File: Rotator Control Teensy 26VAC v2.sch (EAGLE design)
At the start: 61 parts, among them K4 G5LE, K5 G5LE, K6 G5LE, Q1 BSS123, Q2 BSS123, Q3 BSS123

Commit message: add 5V LED, polishing
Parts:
- removed 12VDC, 36VDC, BRAKE, DIR, MOTOR: (no value), led:LED3MM
- removed K4, K5, K6: G5LE, relay:G5LE
- removed R103, R104: 1k, rcl:R-US_R0805
- added K1, K2, K3: G5LE, relay:G5LE
- added LED1: Motor, led:LED3MM
- added LED2: Dir, led:LED3MM
- added LED3: Brake, led:LED3MM
- added LED4: 36V, led:LED3MM
- added LED5: 12V, led:LED3MM
- added LED6: 5V, led:LED3MM
- added R18: 500, rcl:R-US_R0805
- added R19, R20: 1k, rcl:R-US_R0805
- C19: value (none) -> 100u
- C2: device rcl:CPOL-USE7.5-18 -> rcl:CPOL-USE10-22.5
- D4, D5, D6: value (none) -> 1N4148
- X1: value (none) -> Rotor
- X2: value (none) -> 26VAC
- renumbered R102 to R21, U$3 to C19
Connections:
- net N$19 renamed CAP2
- net N$2 renamed N/C
- removed net +5V: U$1.VIN
- new net +12V1: R18.2, U$1.VIN
- new net N$2: LED6.A, R18.1
- net +12V: now also K11.1, K21.1, K31.1; no longer K41.1, K51.1, K61.1
- net +3V3: no longer U$1.3V3_LO
- net 26VAC: now also K12.P, K32.P; no longer K42.P, K62.P
- net BRAKE: now also K32.S; no longer K62.S
- net GND: now also LED4.C, LED5.C, LED6.C; no longer 12VDC.C, 36VDC.C
- net LEFT: now also C4.1, K22.O, R6.1, X1-6.1; no longer C3.1, K52.S, R5.1, X1-5.1
- net N$1: now also R20.2; no longer R104.2
- net N$10: now also K21.2, LED2.C; no longer DIR.C, K51.2
- net N$11: now also K31.2, LED3.C; no longer BRAKE.C, K61.2
- net N$15: now also LED4.A; no longer 36VDC.A
- net N$16: now also LED5.A; no longer 12VDC.A
- net N$3: now also R19.2; no longer R103.2
- net N$4: now also LED1.A; no longer MOTOR.A
- net N$5: now also LED2.A; no longer DIR.A
- net N$6: now also LED3.A; no longer BRAKE.A
- net N$8: now also K12.S, K22.P; no longer K42.S, K52.P
- net N$9: now also K11.2, LED1.C; no longer K41.2, MOTOR.C
- net RIGHT: now also C3.1, K22.S, R5.1, X1-5.1; no longer C4.1, K52.O, R6.1, X1-6.1
- net WIPER+: now also R19.1; no longer R103.1
- net WIPER-: now also R20.1; no longer R104.1
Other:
- note removed: "Cap 130 uFd"
- moved on the sheet: C13, C14, C15, C16, C17, C18, D2, D3, D4, D5, D6, Q1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

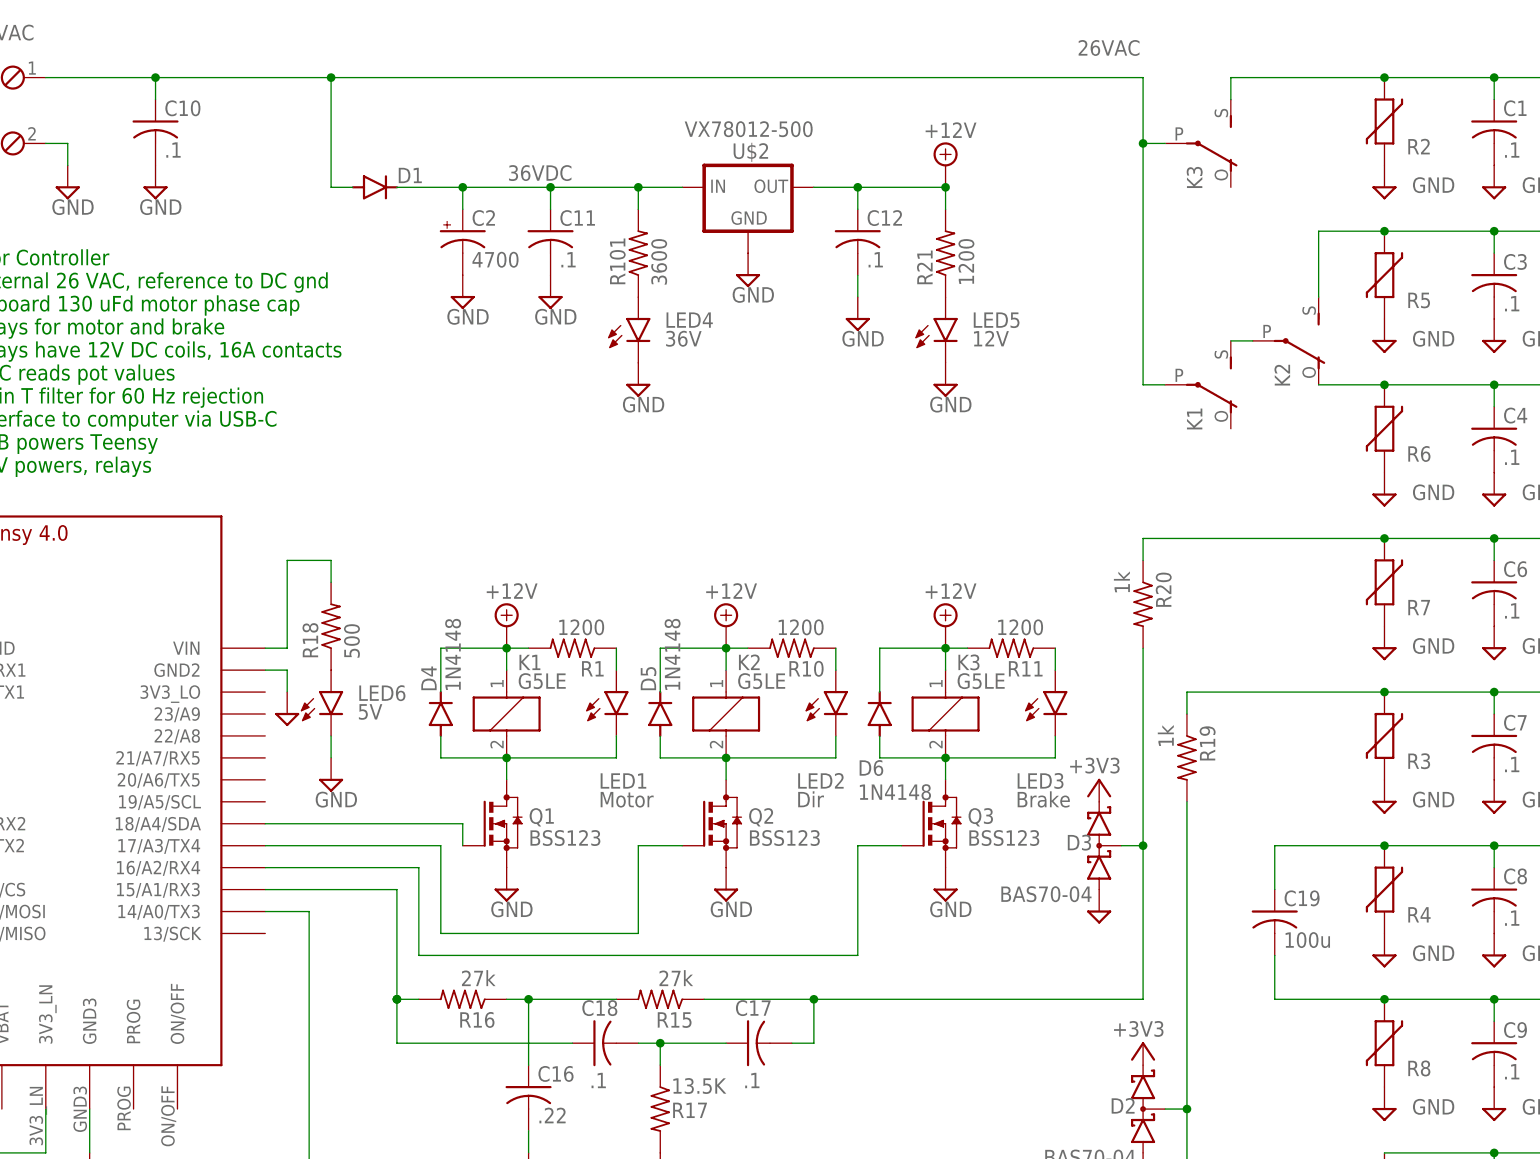
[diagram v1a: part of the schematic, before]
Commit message: Simplified by running relays from 5V from USB 26V AC is only for the rotator
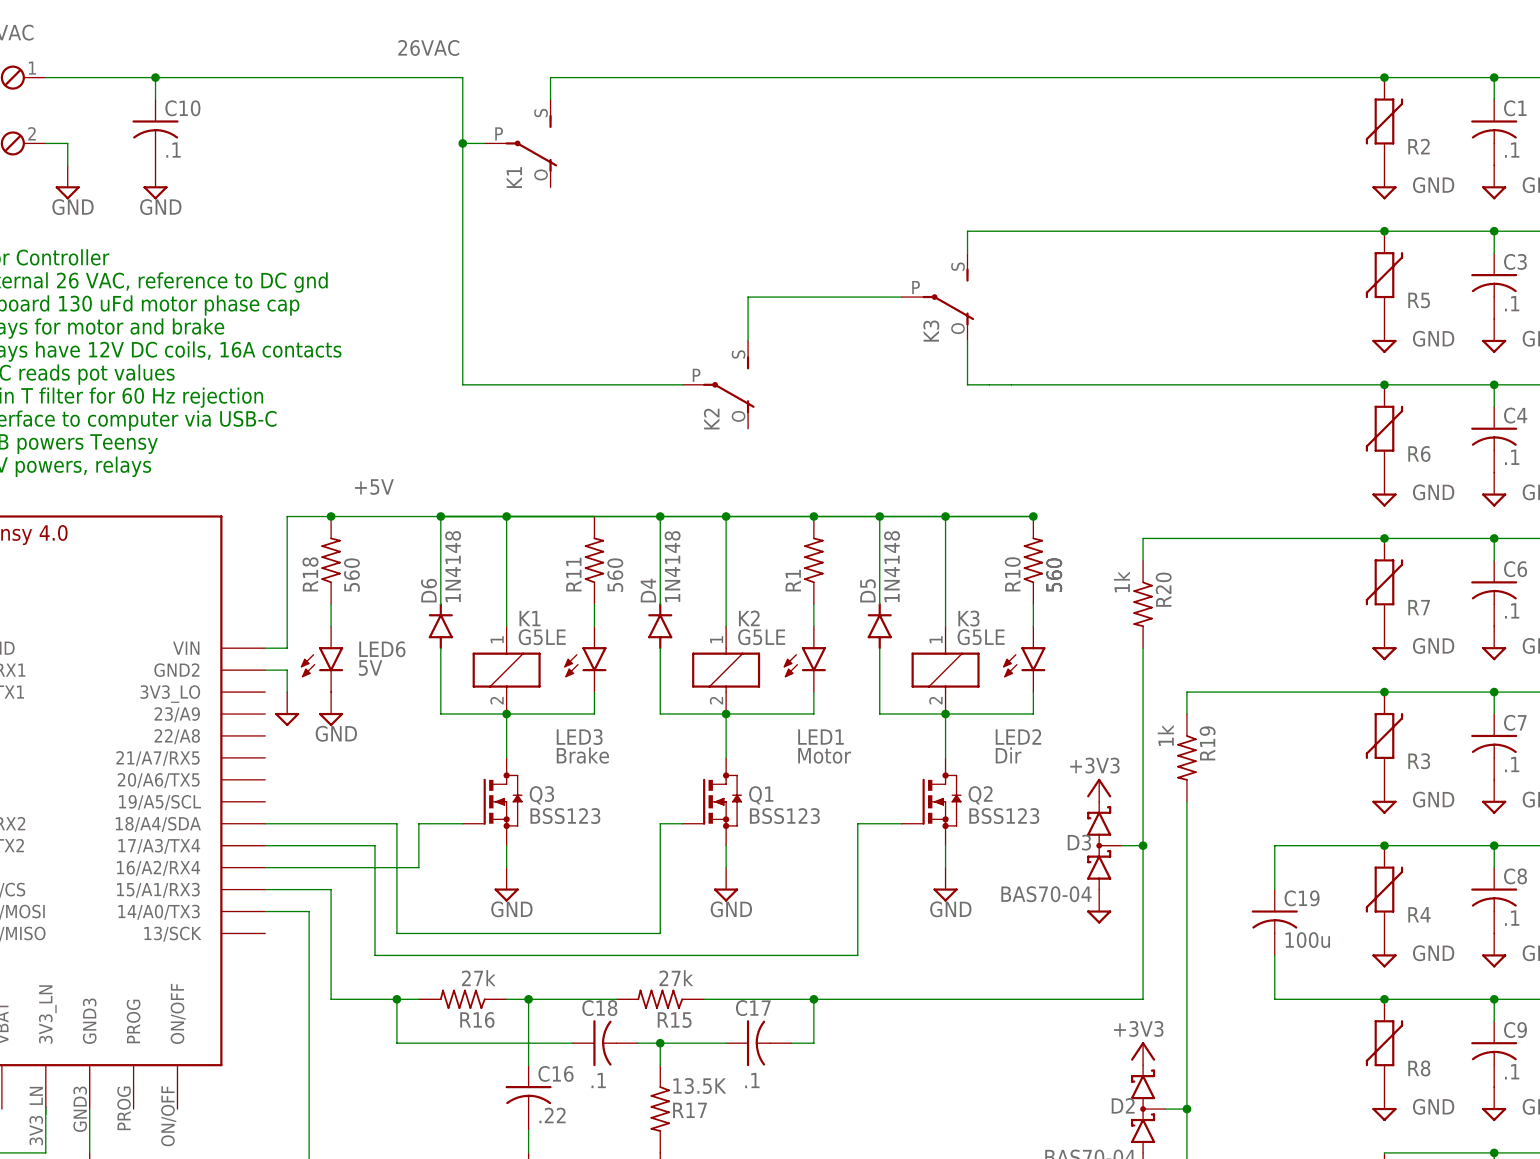
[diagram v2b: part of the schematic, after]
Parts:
- removed C11, C12: .1, rcl:C-USC1206
- removed C2: 4700, rcl:CPOL-USE10-22.5
- removed D1: 1N4148, diode:DIODE-DO214AC
- removed LED4: 36V, led:LED3MM
- removed LED5: 12V, led:LED3MM
- removed R101: 3600, rcl:R-US_R0805
- removed R21: 1200, rcl:R-US_R0805
- removed U$2: VX78012-500, my-library:VX78012-500
- R1, R10, R11: value 1200 -> 560
- R18: value 500 -> 560
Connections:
- removed net +12V: C12.1, D4.C, D5.C, D6.C, K11.1, K21.1, K31.1, R1.2, R10.2, R11.2, R21.2, U$2.OUT
- removed net +12V1: R18.2, U$1.VIN
- removed net 36VDC: C11.1, C2.+, D1.C, R101.2, U$2.IN
- removed net N$15: LED4.A, R101.1
- removed net N$16: LED5.A, R21.1
- new net +5V: D4.C, D5.C, D6.C, K11.1, K21.1, K31.1, R1.2, R10.2, R11.2, R18.2, U$1.VIN
- net 26VAC: now also K22.P; no longer D1.A, K32.P
- net BRAKE: now also K12.S; no longer K32.S
- net GND: no longer C11.2, C12.2, C2.-, LED4.C, LED5.C, U$2.GND
- net LEFT: now also K32.O; no longer K22.O
- net N$10: now also K31.2; no longer K21.2
- net N$11: now also K11.2; no longer K31.2
- net N$8: now also K22.S, K32.P; no longer K12.S, K22.P
- net N$9: now also K21.2; no longer K11.2
- net RIGHT: now also K32.S; no longer K22.S
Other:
- moved on the sheet: D4, D5, D6, K1, K2, K3, LED1, LED2, LED3, LED6, Q1, Q2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

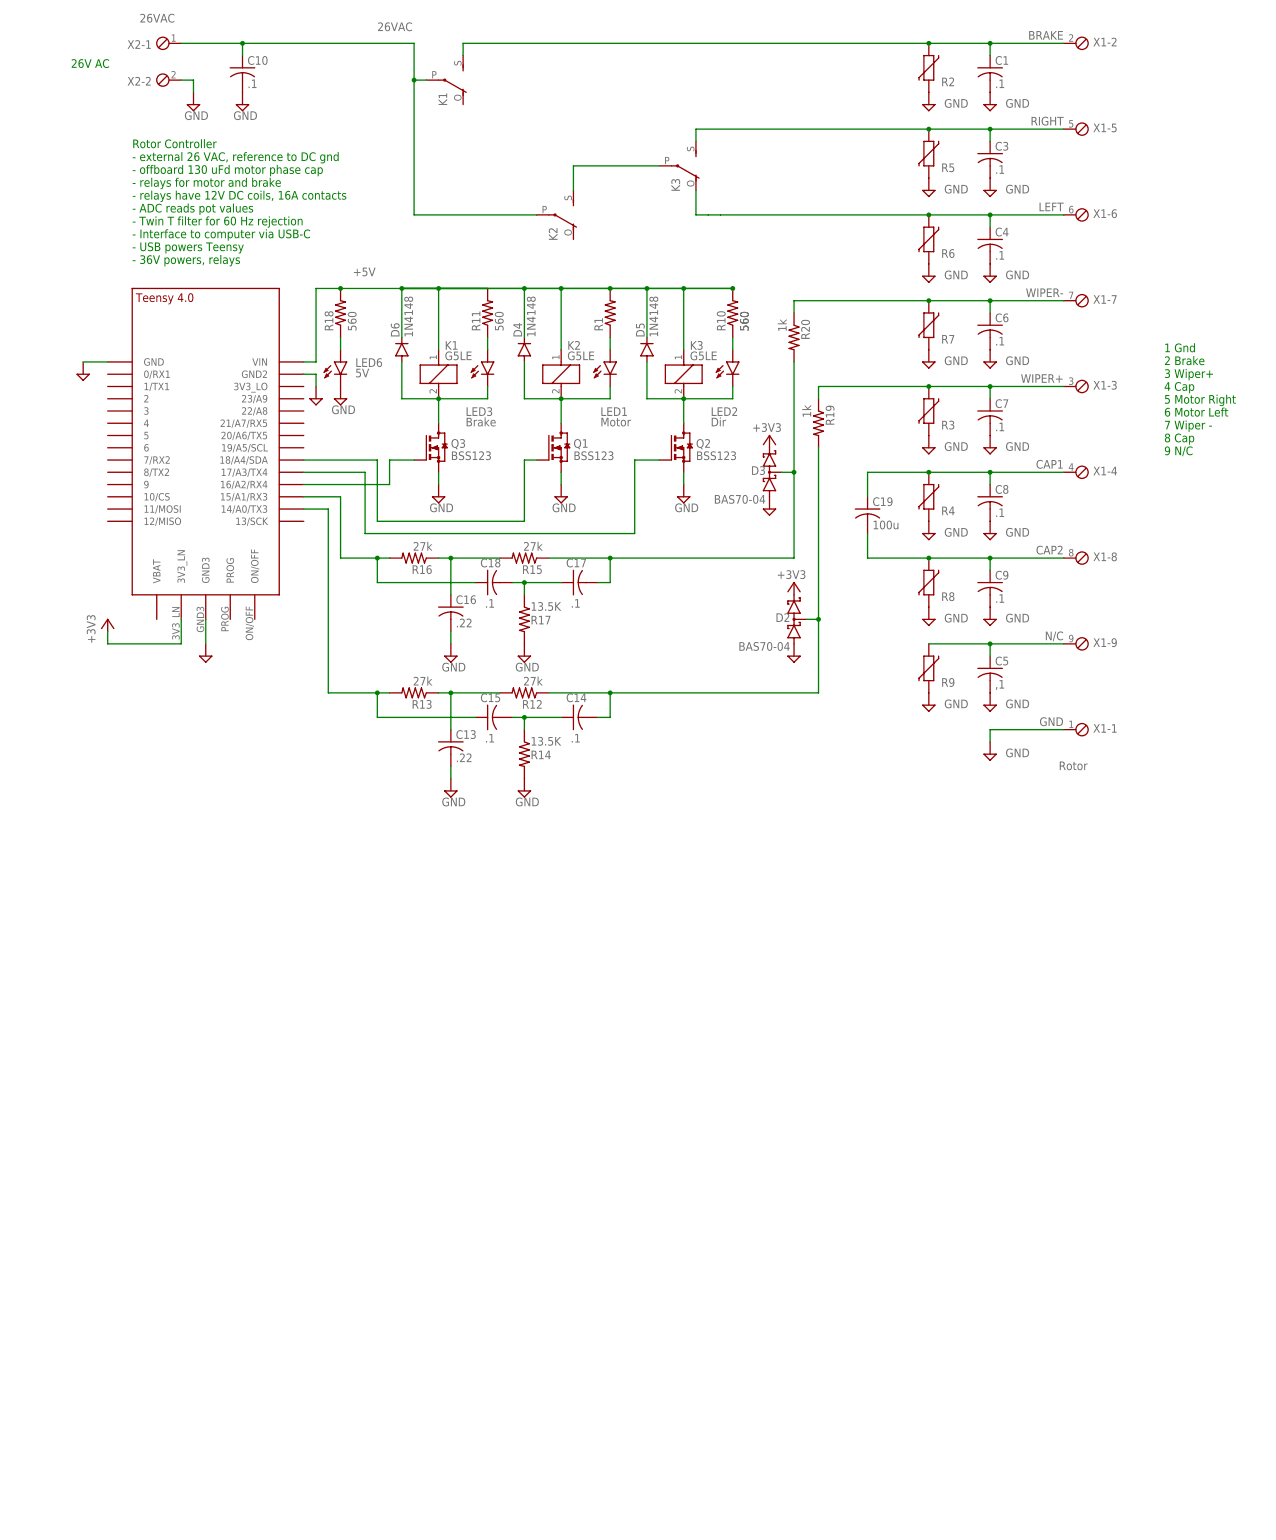
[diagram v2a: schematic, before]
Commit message: switched LED to -.28 inch 4 digit plus driver with keyswitch capability
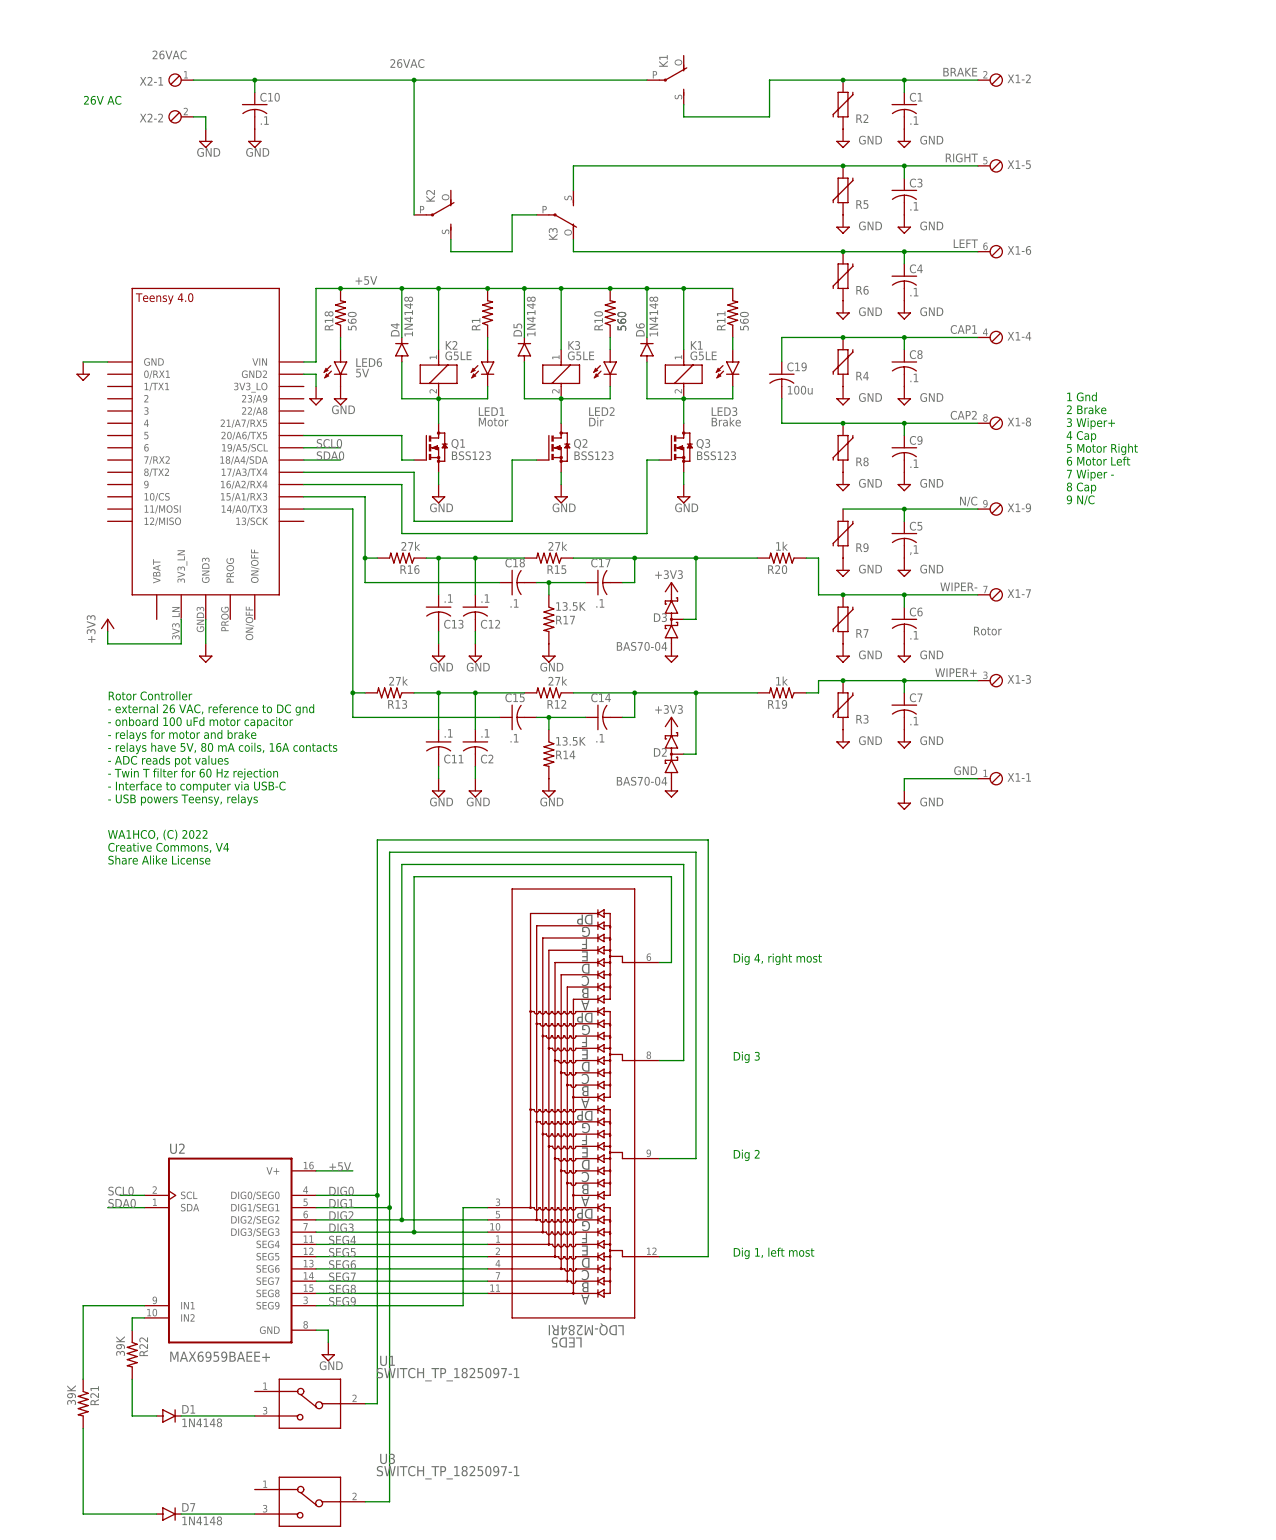
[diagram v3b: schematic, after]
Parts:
- removed C16: .22, rcl:C-USC1206
- added C11, C12, C2: .1, rcl:C-USC1206
- added D1, D7: 1N4148, diode:DIODE-DO214AC
- added LED5: LDQ-M284RI, my-library:LDQ-M284RI
- added R21, R22: 39K, rcl:R-US_R0805
- added U1, U3: SWITCH_TP_1825097-1, my-library:SWITCH_TP_1825097-1
- added U2: MAX6959BAEE+, MAX6959BAEE_:MAX6959BAEE+
- C13: value .22 -> .1
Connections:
- new net DIG0: LED5.12, U1.3, U2.DIG0/SEG0
- new net DIG1: LED5.9, U2.DIG1/SEG1, U3.3
- new net DIG2: LED5.5, LED5.8, U2.DIG2/SEG2
- new net DIG3: LED5.10, LED5.6, U2.DIG3/SEG3
- new net N$15: R21.1, U2.IN1
- new net N$16: R22.1, U2.IN2
- new net N$19: D7.A, R21.2
- new net N$20: D1.A, R22.2
- new net N$24: D1.C, U1.2
- new net N$25: D7.C, U3.2
- new net SCL0: U$1.19/A5/SCL, U2.SCL
- new net SDA0: U$1.18/A4/SDA, U2.SDA
- new net SEG4: LED5.1, U2.SEG4
- new net SEG5: LED5.2, U2.SEG5
- new net SEG6: LED5.4, U2.SEG6
- new net SEG7: LED5.7, U2.SEG7
- new net SEG8: LED5.11, U2.SEG8
- new net SEG9: LED5.3, U2.SEG9
- net +5V: now also U2.V+
- net GND: now also C11.2, C12.2, C2.2, U2.GND; no longer C16.2
- net N$13: now also U$1.20/A6/TX5; no longer U$1.18/A4/SDA
- net N$17: now also C11.1, C2.1; no longer C13.1
- net N$21: now also C12.1, C13.1; no longer C16.1
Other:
- note added: "Dig 1, left most"
- note added: "Dig 2"
- note added: "Dig 3"
- note added: "Dig 4, right most"
- note added: "Rotor Controller - external 26 VAC, reference to DC gnd - onboard 100 uFd motor capacitor - relays for motor and brake - relays have 5V, 80 mA coils, 16A contacts - ADC reads pot values - Twin T filter for 60 Hz rejection - Interface to computer via USB-C - USB powers Teensy, relays"
- note added: "WA1HCO, (C) 2022 Creative Commons, V4 Share Alike License"
- note removed: "Rotor Controller - external 26 VAC, reference to DC gnd - offboard 130 uFd motor phase cap - relays for motor and brake - relays have 12V DC coils, 16A contacts - ADC reads pot values - Twin T filter for 60 Hz rejection - Interface to computer via USB-C - USB powers Teensy - 36V powers, relays"
- moved on the sheet: C1, C10, C13, C14, C15, C17, C18, C19, C3, C4, C5, C6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

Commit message: Released this version to OshPark for fab
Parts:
- removed D7: 1N4148, diode:DIODE-DO214AC
- removed R5, R6, R8, R9: VARISTORCN1206, varistor:VARISTORCN1206
- removed U1, U3: SWITCH_TP_1825097-1, my-library:SWITCH_TP_1825097-1
- added C16: .1, rcl:C-USC1206
- added LED4: 26VAC, led:LED3MM
- added U$2, U$3: SWITCH_AEXIT_6X6X9.5, my-library:SWITCH_AEXIT_6X6X9.5
- D1, D4, D5, D6: device diode:DIODE-DO214AC -> adafruit:DIODESOD-123
- R4: value VARISTORCN1206 -> 3600; device varistor:VARISTORCN1206 -> rcl:R-US_R0805
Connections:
- net +5V: now also C16.1
- net 26VAC: now also D1.A, R2.1
- net BRAKE: no longer R2.1
- net CAP1: no longer R4.1
- net CAP2: no longer R8.1
- net DIG0: now also U$2.P$1, U$3.P$1; no longer U1.3
- net DIG1: no longer U3.3
- net GND: now also C16.2, LED4.C; no longer R4.2, R5.2, R6.2, R8.2, R9.2
- net LEFT: no longer R6.1
- net N$19: now also U$3.P$2; no longer D7.A
- net N$20: now also U$2.P$2; no longer D1.A
- net N$24: now also R4.2; no longer U1.2
- net N$25: now also LED4.A, R4.1; no longer D7.C, U3.2
- net N/C: no longer R9.1
- net RIGHT: no longer R5.1
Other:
- moved on the sheet: C1, C10, C19, C3, C4, C5, C6, C7, C8, C9, LED5, R13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
